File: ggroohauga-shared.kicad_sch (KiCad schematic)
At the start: 13 parts

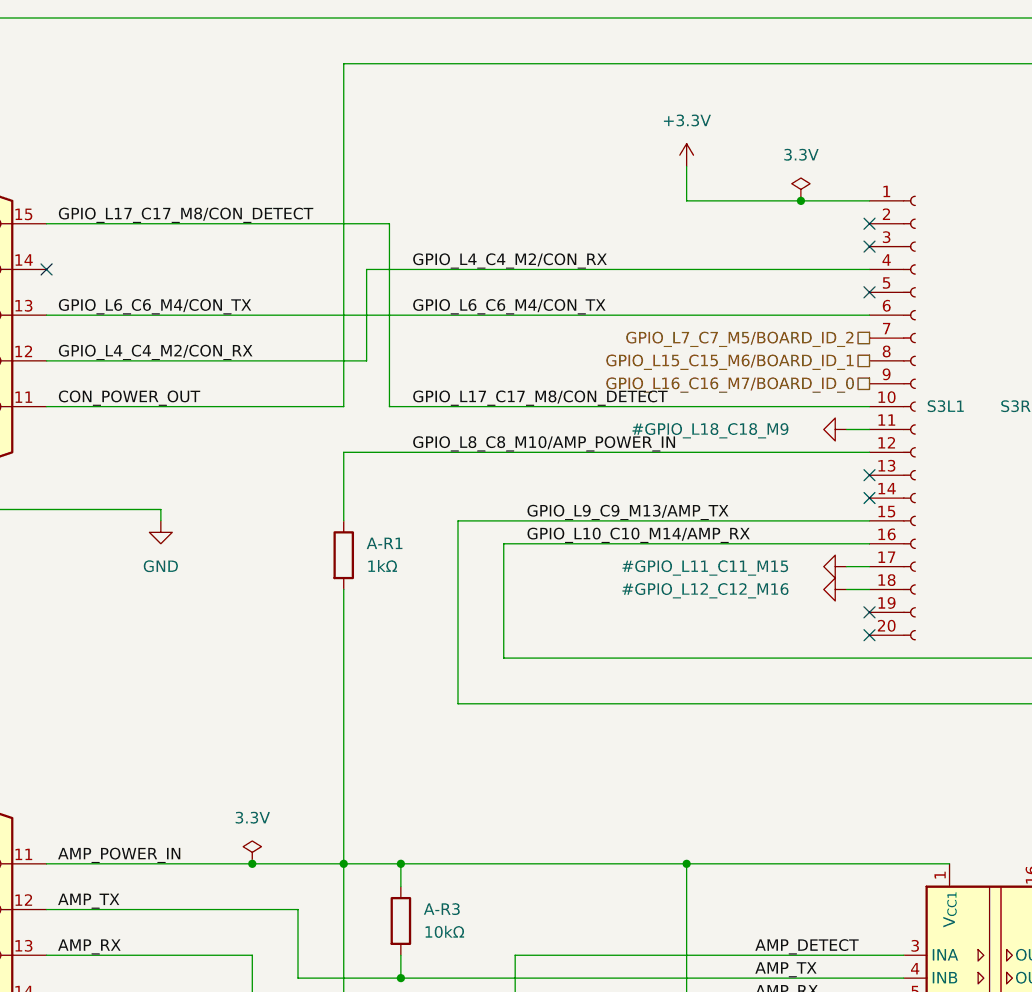
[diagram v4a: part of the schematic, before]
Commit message: Name the two different 3.3V power flags
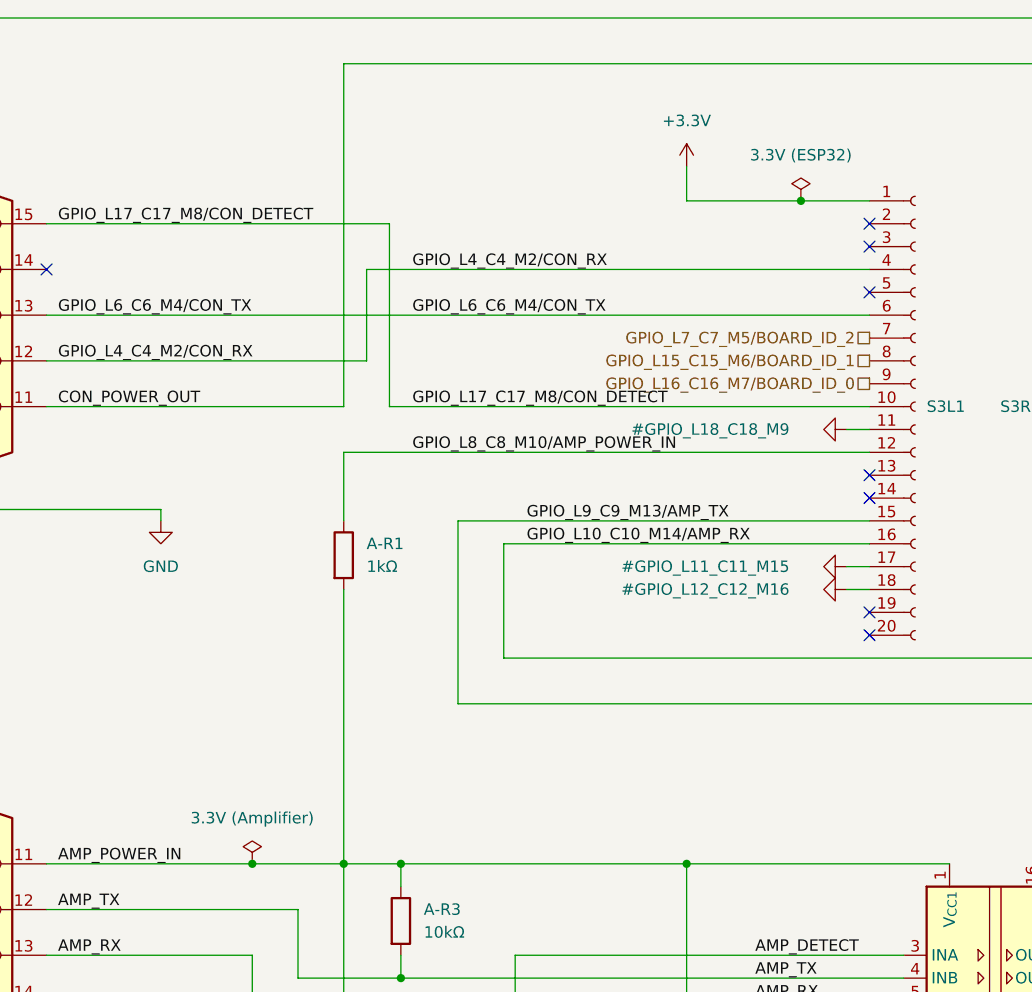
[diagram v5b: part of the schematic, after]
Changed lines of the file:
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@@
 			)
 		)
-		(property "Value" "3.3V"
+		(property "Value" "3.3V (ESP32)"
 			(at 154.94 33.02 0)
 			(effects
@@
 			)
 		)
-		(property "Value" "3.3V"
+		(property "Value" "3.3V (Amplifier)"
 			(at 93.98 106.68 0)
 			(effects
